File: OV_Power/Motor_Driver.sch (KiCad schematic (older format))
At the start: 20 parts, among them CN1 CONN_HEADER_R_A_2POS_2.5MM, U3 LT6106, U4 VNH5019ATR-E

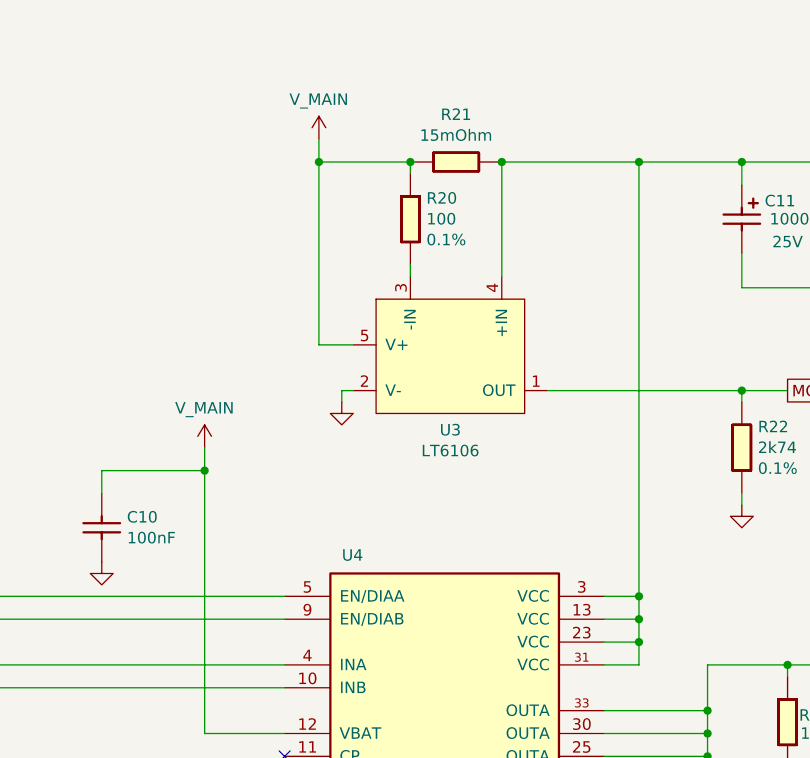
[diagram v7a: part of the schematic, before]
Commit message: Finally getting on with board routing, in TWO layers.  Warning, some things changed on the 20 pin interconnect.
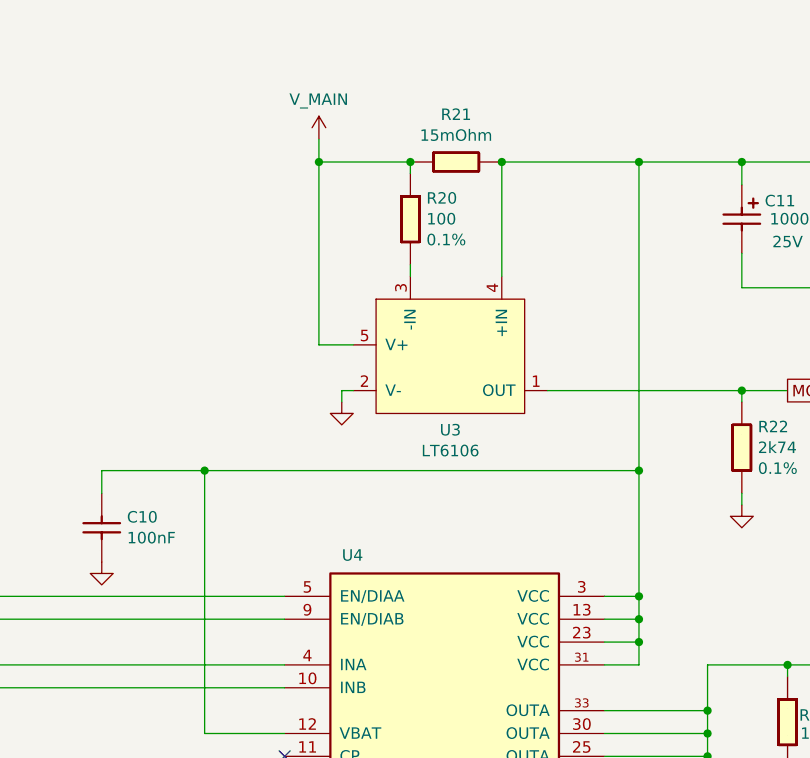
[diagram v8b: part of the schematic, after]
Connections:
- net V_MAIN: no longer C10.1, U4.12 (VBAT)
- net at C11.1 (+), C12.1 (+), C16.1 (+)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: now also C10.1, U4.12 (VBAT)
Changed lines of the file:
@@
 	4200 3650 4550 3650
-Wire Wire Line
-	4200 2400 4200 2500
 Wire Wire Line
 	6400 4500 6400 4350
@@
 	1    0    0    -1
 $EndComp
-$Comp
-L OpenVent:V_MAIN #PWR019
-U 1 1 5FC35966
-P 4200 2400
-F 0 "#PWR019" H 4200 2250 50  0001 C CNN
-F 1 "V_MAIN" H 4200 2573 50  0000 C CNN
-F 2 "" H 4200 2400 50  0001 C CNN
-F 3 "" H 4200 2400 50  0001 C CNN
-	1    4200 2400
-	1    0    0    -1
-$EndComp
 Wire Wire Line
 	2050 3150 4550 3150
@@
 	5500 1150 6100 1150
 Wire Wire Line
-	6100 1150 6100 3050
+	6100 1150 6100 2500
 Connection ~ 6100 3050
 $Comp
@@
 Wire Wire Line
 	3750 2500 4200 2500
-Connection ~ 4200 2500
 Wire Wire Line
 	4200 2500 4200 3650
@@
 Wire Wire Line
 	7650 1700 8200 1700
+Wire Wire Line
+	4200 2500 6100 2500
+Connection ~ 4200 2500
+Connection ~ 6100 2500
+Wire Wire Line
+	6100 2500 6100 3050
 $EndSCHEMATC
